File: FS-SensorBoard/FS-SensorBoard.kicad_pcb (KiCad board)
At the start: 2 copper layers, 100 x 100 mm, 58 parts, among them J1 USB_B, J2 Conn_01x02_Pin, M1 MountingHole, M2 MountingHole, M3 MountingHole, M4 MountingHole, U1 CH340C, U2 ESP32-WROOM-32, U3 TJA1051TK-3, U4 LM2576S-3.3, U5 LM2576S-5

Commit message: Version1
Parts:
- moved R8 155.9 mm to (93.5, 55.9), turned to -90 degrees
- moved U3 155.3 mm to (115.1, 70.9), turned to 90 degrees
- moved LV_Volt1 153.9 mm to (93.5, 49.3)
- moved R2 150.8 mm to (95.1, 59.7)
- moved R1 149.4 mm to (96.6, 55.9), turned to 90 degrees
- moved LV_Temp1 144.8 mm to (103.7, 49.3)
- moved R3 143.0 mm to (103.6, 55.9), turned to 90 degrees
- moved C8 139.3 mm to (118.1, 70.9), turned to -90 degrees
- moved R21 125.0 mm to (136.6, 48.8)
- moved CAN_1 123.0 mm to (116.3, 65.3), turned to 180 degrees
- moved C3 116.8 mm to (139.7, 45.5)
- moved Accelerometer1 115.6 mm to (123.2, 81.5)
- moved C4 115.0 mm to (140.9, 40.4), turned to 180 degrees
- moved C5 114.9 mm to (140.9, 42.9), turned to 180 degrees
- moved U1 104.0 mm to (168.4, 45.0), turned to 180 degrees
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- renumbered J2 to CAN_1, M1 to M3_1, M2 to M3_2, M3 to M3_3, M4 to M3_4
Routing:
- net +5V: track 9.15 -> 128.7 mm, vias 0 -> 5
- net +3V3: track 8.96 -> 127.2 mm, vias 0 -> 3
- net /I2C_1: track 0.00 -> 77.3 mm, vias 0 -> 1
- net /ADC2_6: track 2.55 -> 74.6 mm
- net /I2C_2: track 0.00 -> 70.7 mm, vias 0 -> 1
- net /ADC1_0: track 0.00 -> 69.4 mm
- net /ADC1_4: track 2.56 -> 66.3 mm
- net /ADC2_5: track 2.54 -> 63.9 mm
- net /ADC1_3: track 0.00 -> 56.1 mm
- net /ADC2_4: track 2.54 -> 57.8 mm
- net /ADC1_5: track 2.54 -> 55.3 mm
- net /CAN_TX: track 0.00 -> 48.0 mm
- net /CAN_RX: track 0.00 -> 46.2 mm
- net /ADC1_6: track 2.54 -> 36.1 mm
- net /ADC2_7: track 2.54 -> 30.7 mm
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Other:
- board size 100 x 100 mm -> 97 x 70 mm

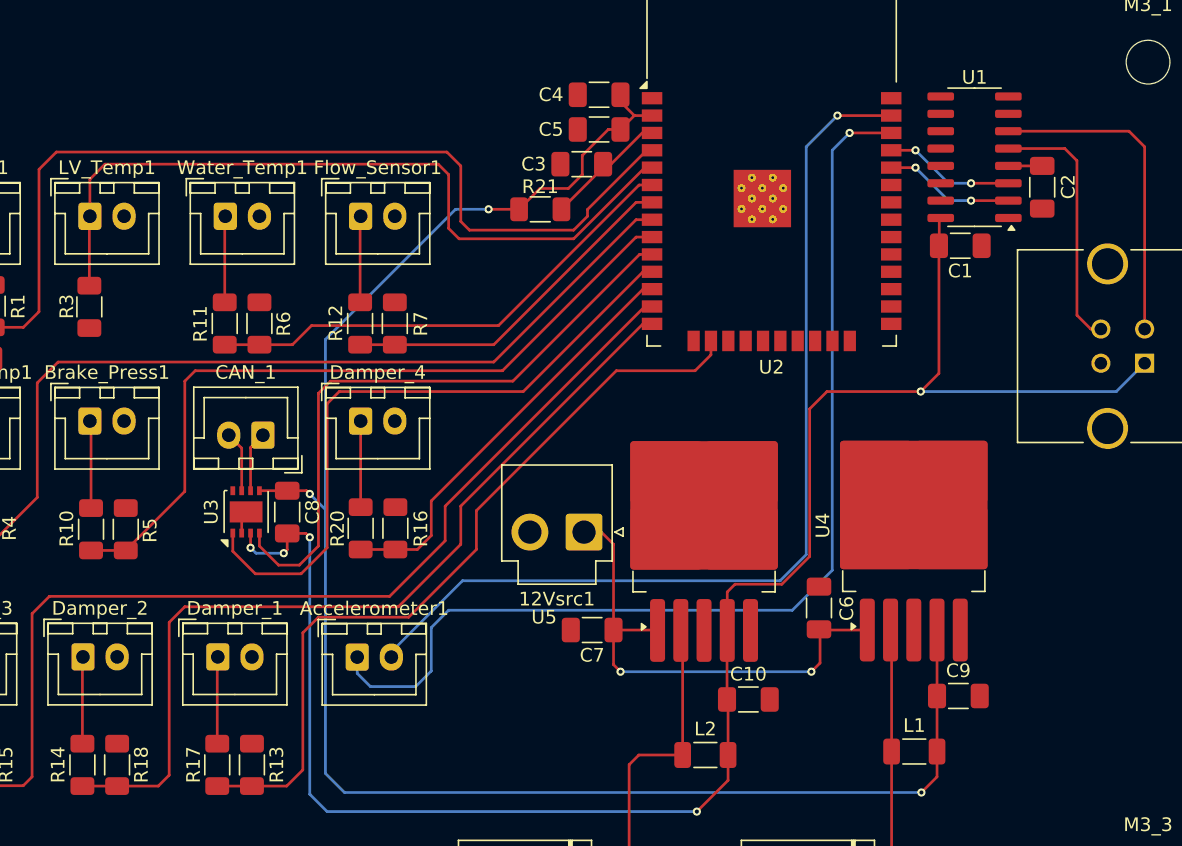
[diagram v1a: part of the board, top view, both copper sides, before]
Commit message: Add silkscreens
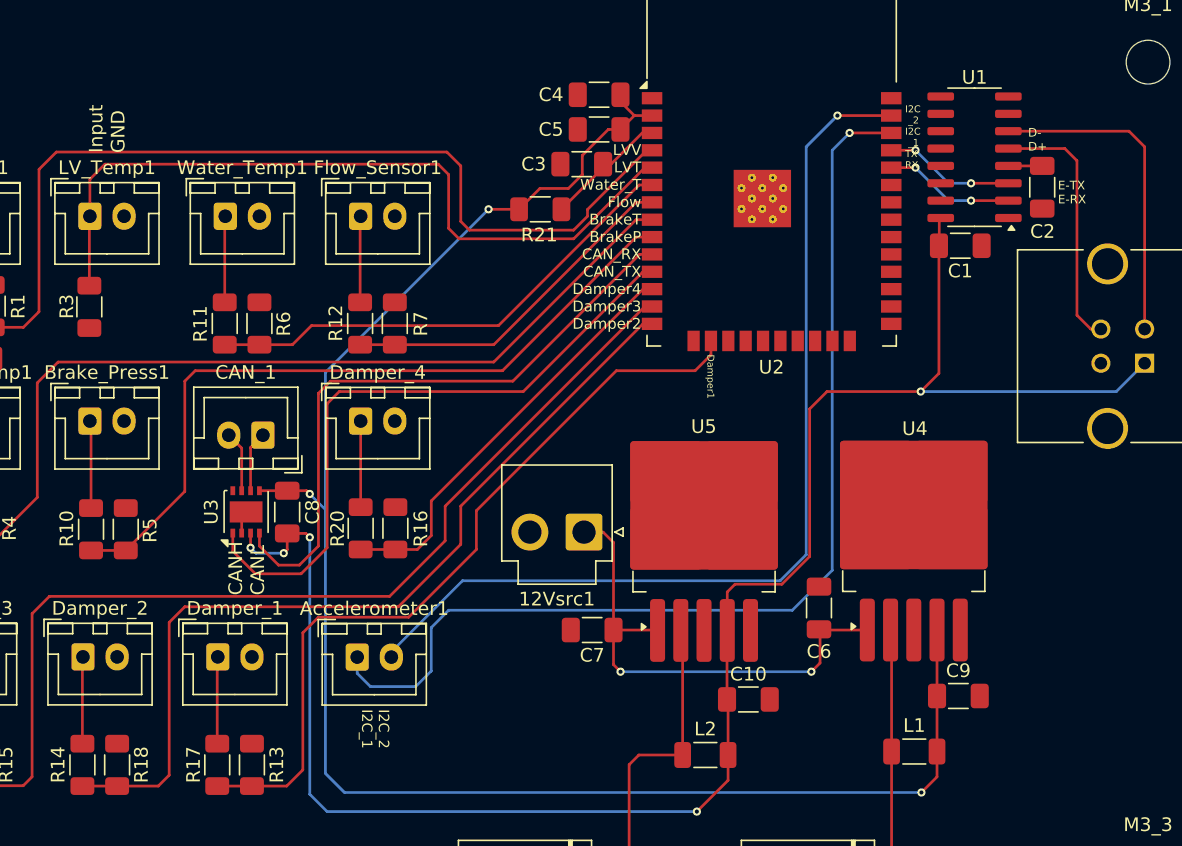
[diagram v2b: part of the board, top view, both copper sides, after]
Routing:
- net +3V3: track 127.2 -> 125.8 mm
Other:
- board text added: "CANH CANL"
- board text added: "D- D+"
- board text added: "Damper1"
- board text added: "E-TX E-RX"
- board text added: "I2C _2 I2C _1 TX RX"
- board text added: "I2C_2 I2C_1"
- board text added: "Input GND"
- board text added: "LVV LVT Water_T Flow BrakeT BrakeP CAN_RX CAN_TX Damper4 Damper3 Damper2"
